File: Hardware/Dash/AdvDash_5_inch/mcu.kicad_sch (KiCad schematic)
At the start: 19 parts, among them J6 AUX, J6 UART0, SW1 RESET, SW2 RESET, U1 ESP32-S3-WROOM-1, U1 PC817, U7 PC817

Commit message: PCB R0.1.0
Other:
- company: (none) -> ADV.ECU - GNVPerformance
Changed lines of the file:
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@@
 (kicad_sch (version 20230121) (generator eeschema)
   (paper "A4")
+  (title_block
+    (date "2023-10-27")
+    (rev "0.1.0")
+    (company "ADV.ECU - GNVPerformance")
+  )
   (junction (at 81.915 159.385) (diameter 0) (color 0 0 0 0)
   )
@@
     (fill (type none))
   )
+  (text_box "R35 and R36 are pull-up resistors in case the mcu in deep sleep does not have pull-ups"
+    (at 93.345 139.065 0) (size 27.305 10.795)
+    (stroke (width 0) (type default))
+    (fill (type none))
+    (effects (font (size 1.27 1.27)) (justify left top))
+  )
   (text "Free GPIO" (at 238.76 163.195 0)

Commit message: :adhesive_bandage: Minor change to the PCB
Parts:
- C18: LCSC (none) -> C15850
- C19: LCSC (none) -> C38141
- R22, R4: LCSC (none) -> C17530
- R29, R31, R4: LCSC (none) -> C17414
- SW1, SW2: LCSC (none) -> C2886898
- U1: LCSC (none) -> C2913199
- U1, U7: LCSC (none) -> C3025164
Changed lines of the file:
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@@
       (effects (font (size 1.27 1.27)) (justify left bottom) hide)
+    )
+    (property "LCSC" "C2886898" (at 235.585 61.595 0)
+      (effects (font (size 1.27 1.27)) hide)
     )
     (pin "1")
@@
     )
     (property "Datasheet" "https://www.espressif.com/sites/default/files/documentation/esp32-s3-wroom-1_wroom-1u_datasheet_en.pdf" (at 148.59 132.08 0)
+      (effects (font (size 1.27 1.27)) hide)
+    )
+    (property "LCSC" "C2913199" (at 146.05 81.28 0)
       (effects (font (size 1.27 1.27)) hide)
     )
@@
       (effects (font (size 1.27 1.27)) hide)
     )
+    (property "LCSC" "C17414" (at 75.565 153.67 0)
+      (effects (font (size 1.27 1.27)) hide)
+    )
     (pin "1")
     (pin "2")
@@
       (effects (font (size 1.27 1.27)) hide)
     )
+    (property "LCSC" "C17414" (at 219.71 48.26 0)
+      (effects (font (size 1.27 1.27)) hide)
+    )
     (pin "1")
     (pin "2")
@@
     )
     (property "Datasheet" "~" (at 153.035 30.48 0)
+      (effects (font (size 1.27 1.27)) hide)
+    )
+    (property "LCSC" "C15850" (at 153.035 30.48 0)
       (effects (font (size 1.27 1.27)) hide)
     )
@@
     (property "MANUFACTURER" "E SWITCH" (at 66.675 45.72 0)
       (effects (font (size 1.27 1.27)) (justify left bottom) hide)
+    )
+    (property "LCSC" "C2886898" (at 66.675 45.72 0)
+      (effects (font (size 1.27 1.27)) hide)
     )
     (pin "1")
@@
       (effects (font (size 1.27 1.27)) hide)
     )
+    (property "LCSC" "C17414" (at 147.955 155.575 0)
+      (effects (font (size 1.27 1.27)) hide)
+    )
     (pin "1")
     (pin "2")
@@
       (effects (font (size 1.27 1.27)) hide)
     )
+    (property "LCSC" "C17414" (at 94.615 35.56 0)
+      (effects (font (size 1.27 1.27)) hide)
+    )
     (pin "1")
     (pin "2")
@@
       (effects (font (size 1.27 1.27)) hide)
     )
+    (property "LCSC" "C38141" (at 140.335 30.48 0)
+      (effects (font (size 1.27 1.27)) hide)
+    )
     (pin "1")
     (pin "2")
@@
     )
     (property "Datasheet" "~" (at 121.92 161.29 0)
+      (effects (font (size 1.27 1.27)) hide)
+    )
+    (property "LCSC" "C17530" (at 121.92 161.29 0)
       (effects (font (size 1.27 1.27)) hide)
     )
@@
       (effects (font (size 1.27 1.27)) (justify left) hide)
     )
+    (property "LCSC" "C3025164" (at 134.62 163.83 0)
+      (effects (font (size 1.27 1.27)) hide)
+    )
     (pin "1")
     (pin "2")
@@
       (effects (font (size 1.27 1.27)) hide)
     )
+    (property "LCSC" "C17530" (at 50.8 159.385 0)
+      (effects (font (size 1.27 1.27)) hide)
+    )
     (pin "1")
     (pin "2")
@@
       (effects (font (size 1.27 1.27)) (justify left) hide)
     )
-    (pin "1")
+    (property "LCSC" "C3025164" (at 63.5 161.925 0)
+      (effects (font (size 1.27 1.27)) hide)
+    )
+    (pin "1")

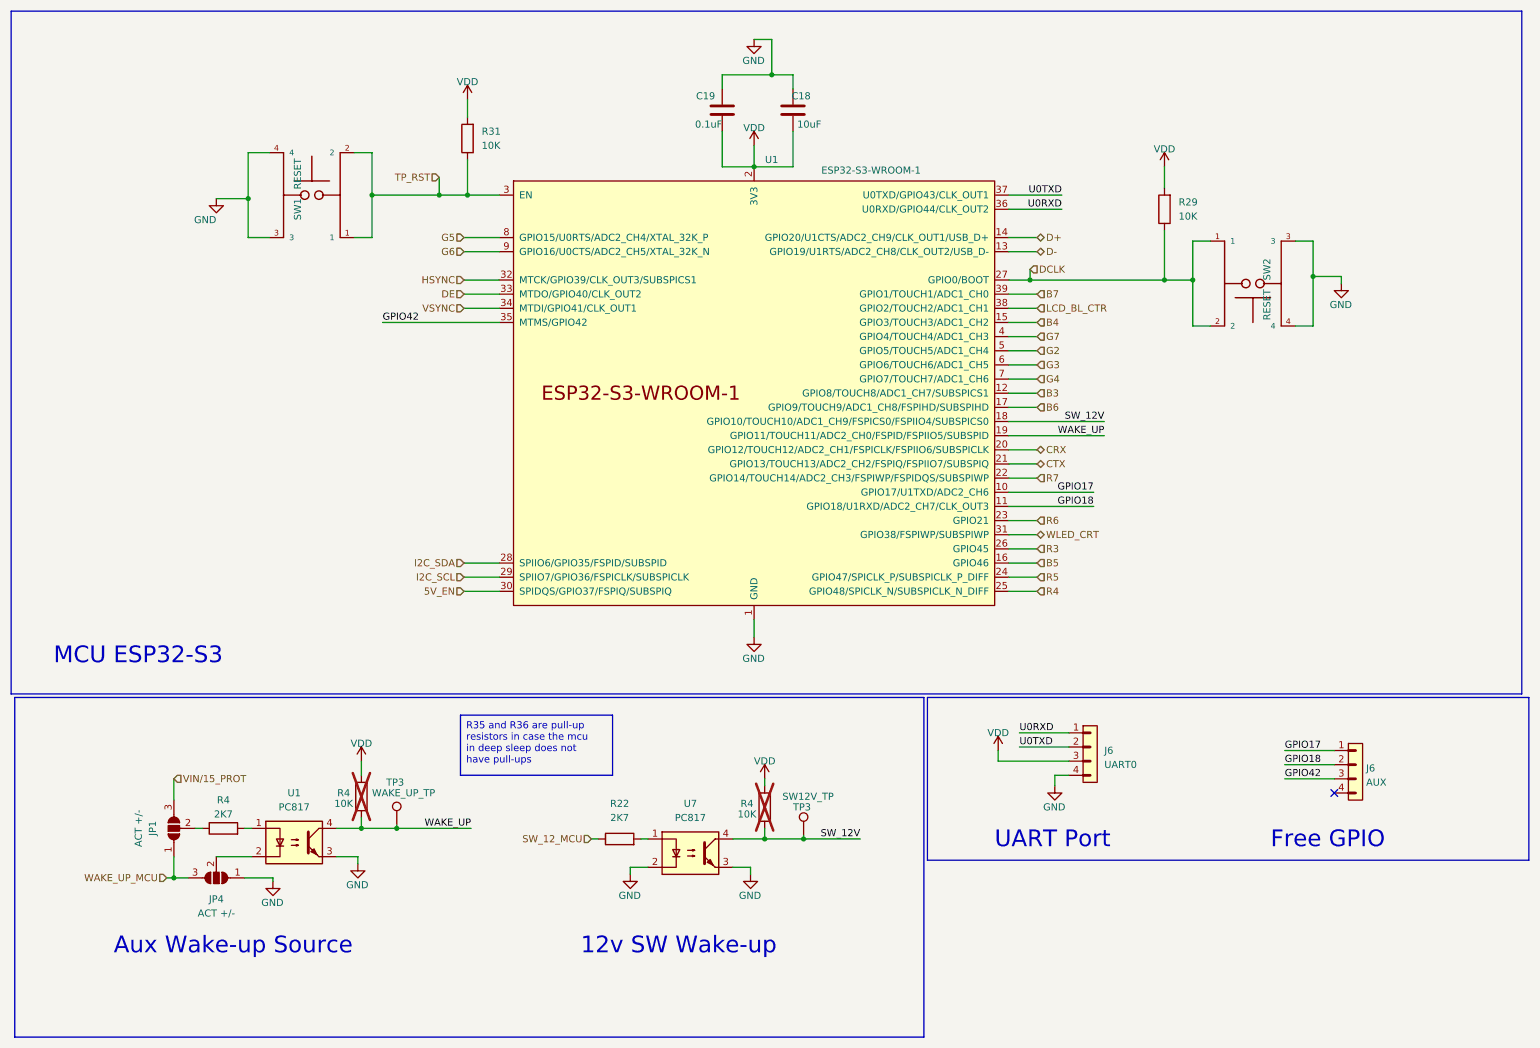
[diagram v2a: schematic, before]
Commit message: :adhesive_bandage: Fix errors in pcb desing, changelog in file, rev0.2.0
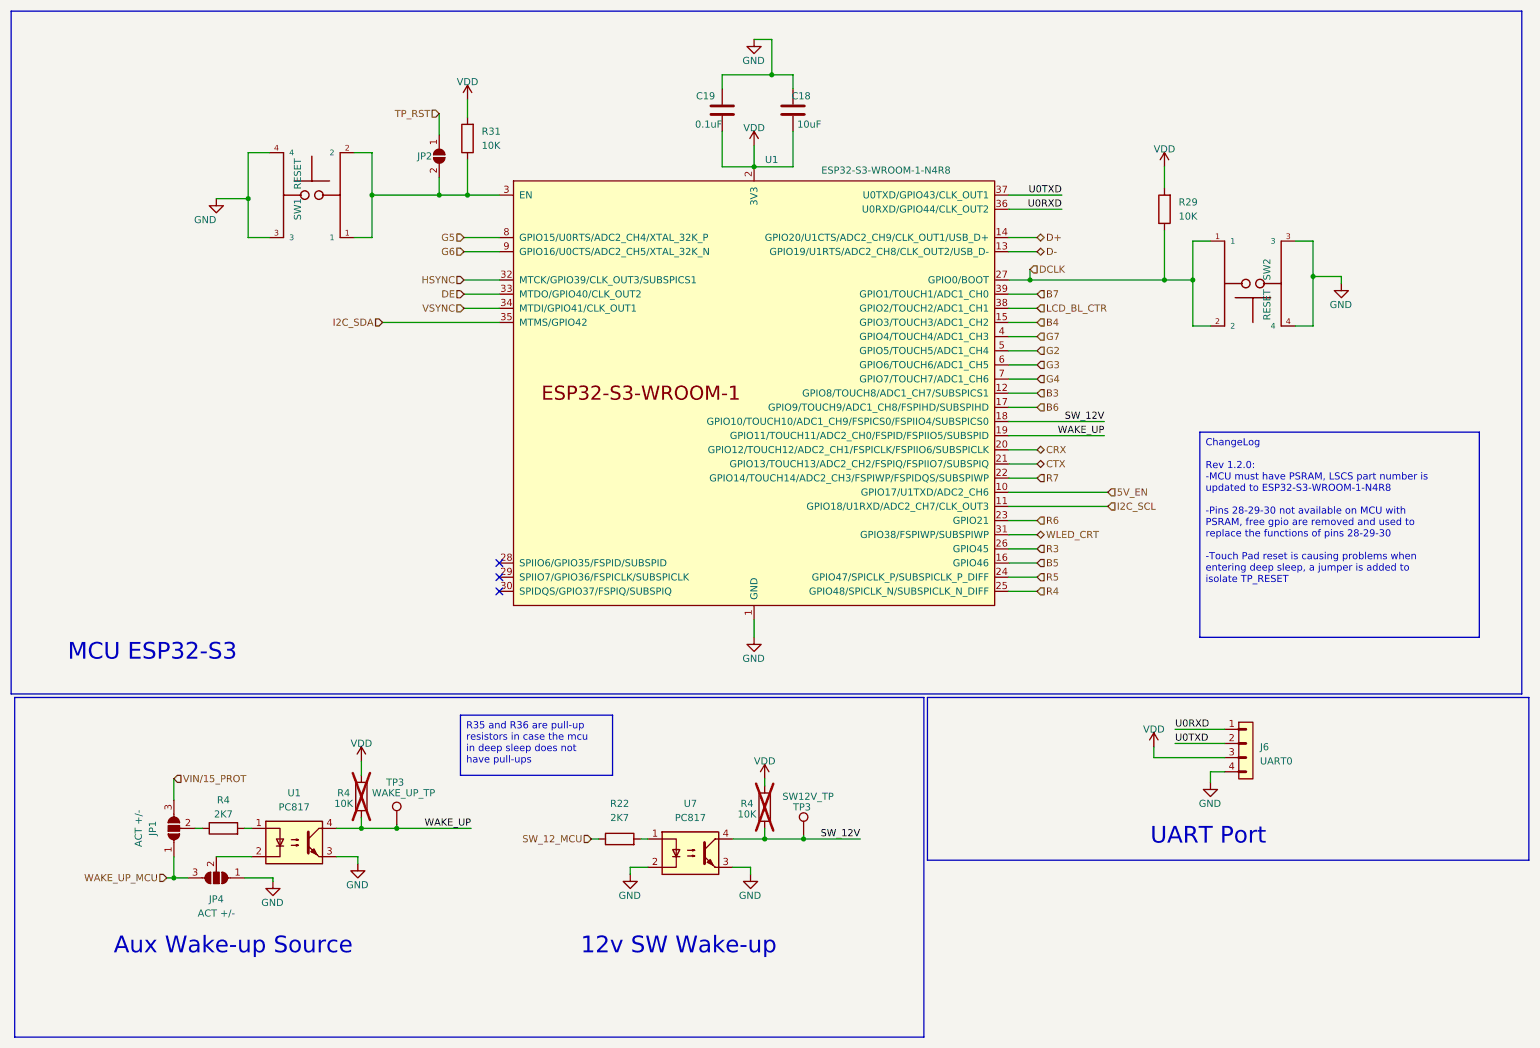
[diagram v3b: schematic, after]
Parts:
- removed J6: AUX, Connector_PinHeader_2.54mm:PinHeader_1x04_P2.54mm_Vertical_SMD_Pin1Left, symbol PCM_SL_Pin_Headers:PINHD_1x4_Male
- added JP2: 120ohm, Jumper:SolderJumper-2_P1.3mm_Open_TrianglePad1.0x1.5mm, symbol Jumper:SolderJumper_2_Open
- U1: value ESP32-S3-WROOM-1 -> ESP32-S3-WROOM-1-N4R8; LCSC C2913199 -> C2913200
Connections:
- net GPIO17 is gone; now on net 5V_EN: U1.10 (GPIO17/U1TXD/ADC2_CH6)
- net GPIO18 is gone; now on net I2C_SCL: U1.11 (GPIO18/U1RXD/ADC2_CH7/CLK_OUT3)
- net GPIO42 is gone; now on net I2C_SDA: U1.35 (MTMS/GPIO42)
- net 5V_EN: no longer U1.30 (SPIDQS/GPIO37/FSPIQ/SUBSPIQ)
- net I2C_SCL: no longer U1.29 (SPIIO7/GPIO36/FSPICLK/SUBSPICLK)
- net I2C_SDA: no longer U1.28 (SPIIO6/GPIO35/FSPID/SUBSPID)
- net TP_RST: now also JP2.1 (A); no longer R31.1, SW1.1, SW1.2, U1.3 (EN)
- new net: JP2.2 (B), R31.1, SW1.1, SW1.2, U1.3 (EN)
- no-connect marks 1 -> 3
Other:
- note removed: "Free GPIO"
- moved on the sheet: J6

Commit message: :bug: PCB R0.2.0 Ready, change log in kicad files
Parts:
- removed JP2: 120ohm, Jumper:SolderJumper-2_P1.3mm_Open_TrianglePad1.0x1.5mm, symbol Jumper:SolderJumper_2_Open
- added JP1 (x2): ACT +/-, Jumper:SolderJumper-3_P1.3mm_Open_Pad1.0x1.5mm, symbol Jumper:SolderJumper_3_Open
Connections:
- net CRX: now also JP1.1 (A); no longer U1.20 (GPIO12/TOUCH12/ADC2_CH1/FSPICLK/FSPIIO6/SUBSPICLK)
- net CTX: now also JP1.1 (A); no longer U1.21 (GPIO13/TOUCH13/ADC2_CH2/FSPIQ/FSPIIO7/SUBSPIQ)
- net I2C_SCL: now also U1.35 (MTMS/GPIO42); no longer U1.11 (GPIO18/U1RXD/ADC2_CH7/CLK_OUT3)
- net I2C_SDA: now also U1.31 (GPIO38/FSPIWP/SUBSPIWP); no longer U1.35 (MTMS/GPIO42)
- net TP_RST: now also R31.1, SW1.1, SW1.2, U1.3 (EN)
- net U0RXD: now also JP1.3 (B); no longer U1.36 (U0RXD/GPIO44/CLK_OUT2)
- net U0TXD: now also JP1.3 (B); no longer U1.37 (U0TXD/GPIO43/CLK_OUT1)
- net WLED_CRT: now also U1.21 (GPIO13/TOUCH13/ADC2_CH2/FSPIQ/FSPIIO7/SUBSPIQ); no longer U1.31 (GPIO38/FSPIWP/SUBSPIWP)
- new net: JP1.2 (C), U1.36 (U0RXD/GPIO44/CLK_OUT2)
- new net: JP1.2 (C), U1.37 (U0TXD/GPIO43/CLK_OUT1)
- new net TP_RST_2: U1.11 (GPIO18/U1RXD/ADC2_CH7/CLK_OUT3)
- new net WLED_CLK: U1.20 (GPIO12/TOUCH12/ADC2_CH1/FSPICLK/FSPIIO6/SUBSPICLK)

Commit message: 🚀 PCB R0.2.1
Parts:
- renumbered J6 to J5, TP3 to TP8, TP3 to TP9
